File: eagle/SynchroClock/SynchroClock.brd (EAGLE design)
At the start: 84.8 x 45.7 mm, 38 parts, among them IC1 MCP1702-18, IC2 DS3231/SO, J1 VIN, U1 TC1262, U2 DRV8838, U3 ATTINY85-P

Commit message: switch to 1.5v for clock voltage regulator
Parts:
- IC1: value MCP1702-18 -> MCP1702-15
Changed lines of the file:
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@@
 <?xml version="1.0" encoding="utf-8"?>
 <!DOCTYPE eagle SYSTEM "eagle.dtd">
-<eagle version="8.2.1">
+<eagle version="8.2.2">
 <drawing>
 <settings>
@@
 <element name="C9" library="capacitor-wima" library_urn="urn:adsk.eagle:library:116" package="C2.5-2" value="0.1uf" x="31.75" y="17.78" rot="R90"/>
 <element name="IC2" library="SynchroClock" package="SO16W" value="DS3231/SO" x="77.47" y="15.24"/>
-<element name="IC1" library="SynchroClock" package="TO92-INLINE" value="MCP1702-18" x="12.7" y="8.89"/>
+<element name="IC1" library="SynchroClock" package="TO92-INLINE" value="MCP1702-15" x="12.7" y="8.89"/>
 <element name="JP2" library="pinhead" library_urn="urn:adsk.eagle:library:325" package="1X02" value="CLOCK" x="29.21" y="3.81" rot="R180"/>
 <element name="LED1" library="led" library_urn="urn:adsk.eagle:library:259" package="LED3MM" value="RED" x="3.81" y="34.29"/>

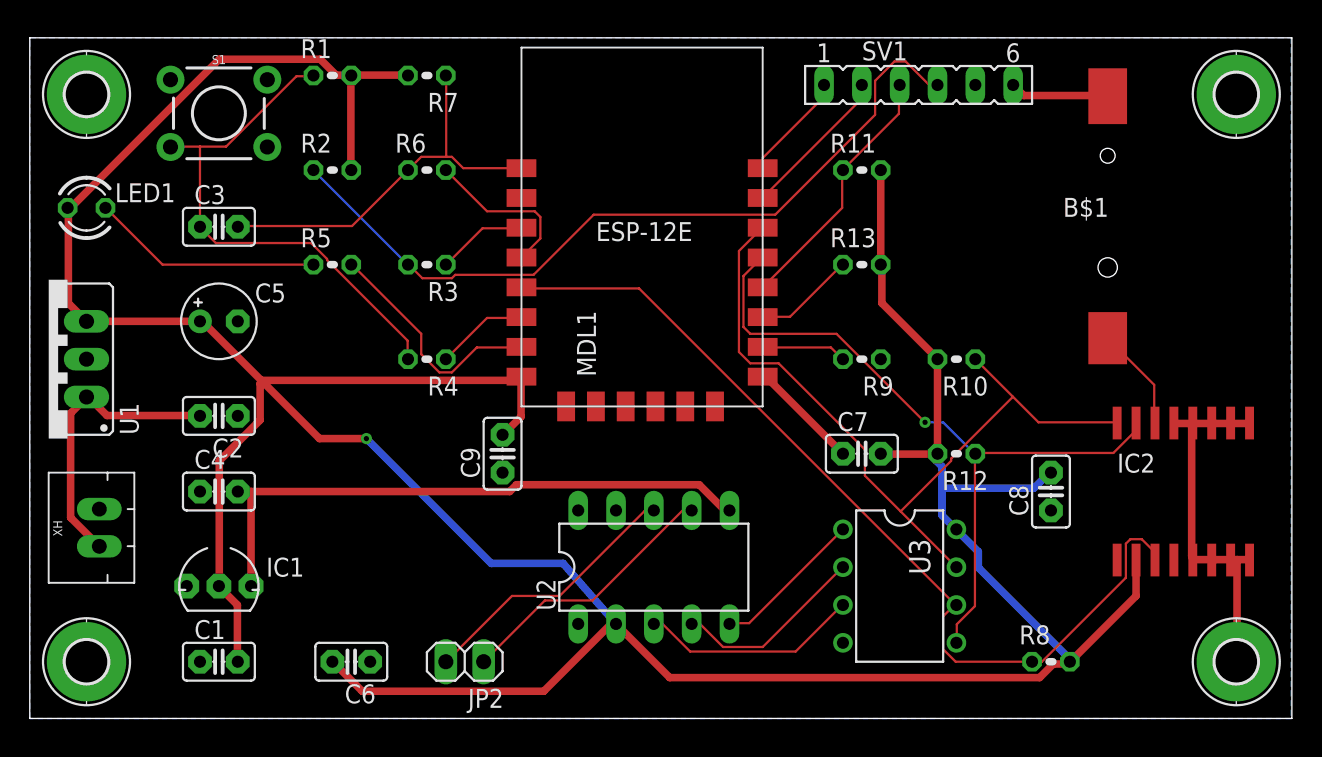
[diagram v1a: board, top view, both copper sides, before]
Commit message: "development" version - board that does not have the clock driver
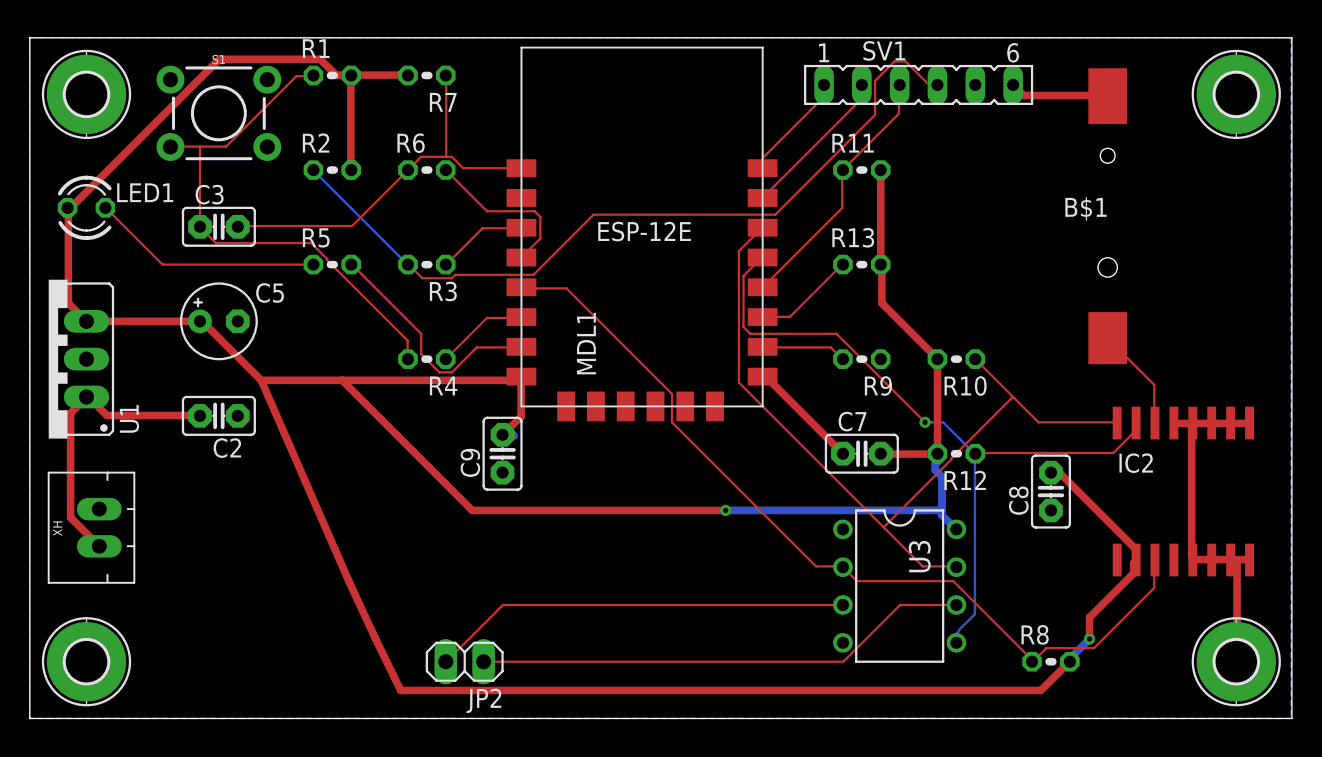
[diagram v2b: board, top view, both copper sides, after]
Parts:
- removed C1, C4, C6: 0.1uf, capacitor-wima:C2.5-2
- removed IC1: MCP1702-15, SynchroClock:TO92-INLINE
- removed U2: DRV8838, SynchroClock:DIL10
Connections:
- removed net +1V8: C4.2, IC1.3, U2.6
- removed net EN: U2.3, U3.3
- removed net N$12: JP2.1, U2.7
- removed net N$13: JP2.2, U2.8
- removed net PH: U2.4, U3.2
- removed net SLP: U2.5, U3.1
- removed net VIN: U2.9
- new net A: JP2.1, U3.6
- new net B: JP2.2, U3.3
- net +3V3: no longer C1.2, C6.2, IC1.2, U2.2
- net 1HZ: now also U3.2; no longer U3.6
- net GND: no longer C1.1, C4.1, C6.1, IC1.1, U2.1, U2.10
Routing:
- net +1V8: track 40.3 -> 0.00 mm
- net A: track 0.00 -> 33.3 mm
- net B: track 0.00 -> 28.2 mm
- net N$13: track 18.2 -> 0.00 mm
- net N$12: track 18.2 -> 0.00 mm
- net EN: track 14.8 -> 0.00 mm
- net PH: track 13.0 -> 0.00 mm
- net SLP: track 10.3 -> 0.00 mm
- net 1HZ: track 61.7 -> 58.1 mm
- net +3V3: track 242.0 -> 238.6 mm, vias 1 -> 2
- net SCL: track 52.8 -> 54.5 mm
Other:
- board text added: "SynchroClock 2.0-Dev"
- board text removed: "SynchroClock 1.0"

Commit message: Alpha 2.0 board
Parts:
- removed B$1: CR1220, SynchroClock:HARWIN-CR1220
- removed C7, C8, C9: 0.1uf, capacitor-wima:C2.5-2
- removed IC2: DS3231/SO, SynchroClock:SO16W
- removed U3: ATTINY85-P, SynchroClock:PDIP08_300MIL
- added B1: CR1220, SynchroClock:HARWIN-CR1220
- added C1: 10uf, capacitor-wima:C5B2.5
- added C4, C6: 0.1uf, capacitor-wima:C2.5-2
- added IC1: DS3231/SO, SynchroClock:SO16W
- added ISP1: AVRISP-6, SynchroClock:AVRISP
- added JP1: PWF, SynchroClock:1X02
- added JP3: ATVCC, SynchroClock:1X02
- added R14, R15: 100, resistor:0204V
- added U2: ATTINY85-P, SynchroClock:PDIP08_300MIL
- C3: value 10uf -> 100uf; device capacitor-wima:C2.5-2 -> rcl:E2,5-5
- C5: value 100uf -> 0.1uf; device rcl:E2,5-5 -> capacitor-wima:C2.5-2
- R11: value 10k -> 4.7k
- R12: value 4.7k -> 10k
- R2, R7: value 10k -> 1k
- R3, R6: value 1k -> 10k
- S1: value MOMENTARY-SWITCH-SPST-PTH-6.0MM -> CONFIG
- moved C5 56.7 mm to (68.8, 18.8), turned to 180 degrees
- moved R11 26.3 mm to (39.9, 16.0), turned to 180 degrees
- moved SV1 25.1 mm to (81.5, 30.1), turned to 90 degrees
- moved R12 20.1 mm to (55.9, 36.8), turned to 0 degrees
- moved JP2 14.7 mm to (14.5, 3.56)
- moved R8 14.7 mm to (56.1, 11.7)
- moved R2 14.2 mm to (26.7, 24.1), turned to 180 degrees
- moved R3 12.7 mm to (26.7, 43.2)
- moved R4 12.7 mm to (26.7, 36.8), turned to 0 degrees
- moved R7 12.7 mm to (26.7, 30.5)
- moved R10 9.34 mm to (55.6, 17.5)
- moved C3 6.35 mm to (12.7, 26.7)
- moved R6 6.35 mm to (20.3, 36.8)
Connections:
- net N$10 renamed GPIO2
- net N$8 renamed GPIO15
- removed net N$2: MDL1.4, R6.2
- removed net N$3: MDL1.3, R3.1
- removed net N$4: MDL1.6, R4.1
- removed net N$5: C3.1, R1.1, R4.2, S1.3
- removed net N$7: LED1.K, R5.1
- new net ATVCC: C6.2, JP3.2, U2.8
- new net CFG: MDL1.6, R2.1
- new net CH_PD: MDL1.3, R7.1
- new net GPIO16: MDL1.4, R4.1
- new net LED: LED1.K, MDL1.7
- new net N$11: JP2.2, R15.2
- new net N$9: JP2.1, R14.2
- new net NRES: ISP1.5, JP1.1, U2.1
- new net NRST: IC1.4, JP1.2
- new net REST: C1.2, MDL1.1, R3.1, R4.2
- net +3V3: now also C3.+, C4.2, C5.2, IC1.2, ISP1.2, JP3.1, R3.2, R5.2, R6.2; no longer C5.+, C7.2, C8.2, C9.2, IC2.2, LED1.A, R2.2, R7.2, U3.8
- net 1HZ: now also IC1.3, U2.2; no longer IC2.3, U3.2
- net A: now also ISP1.1, R14.1, U2.6; no longer JP2.1, U3.6
- net B: now also R15.1, U2.3; no longer JP2.2, U3.3
- net GND: now also B1.NEG, C3.-, C4.1, C5.1, C6.1, IC1.10, IC1.11, IC1.12, IC1.13, IC1.5, IC1.6, IC1.7, IC1.8, IC1.9, ISP1.6, U2.4; no longer B$1.NEG, C5.-, C7.1, C8.1, C9.1, IC2.10, IC2.11, IC2.12, IC2.13, IC2.5, IC2.6, IC2.7, IC2.8, IC2.9, U3.4
- net GPIO0: now also R12.1; no longer R11.1
- net N$1: now also C1.1, R1.1, R2.2, S1.3; no longer C3.2, MDL1.1, R6.1, R7.1
- net N$6: now also LED1.A, R5.1; no longer MDL1.7, R5.2
- net RST: now also R6.1, R7.2; no longer R2.1, R3.2
- net SCL: now also IC1.16, ISP1.3, U2.7; no longer IC2.16, U3.7
- net SDA: now also IC1.15, ISP1.4, R11.1, U2.5; no longer IC2.15, R12.1, U3.5
- net VBAT: now also B1.POS, IC1.14; no longer B$1.POS, IC2.14
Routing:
- net +3V3: track 238.6 -> 149.3 mm, vias 2 -> 0
- net SDA: track 49.5 -> 95.6 mm
- net GPIO0: track 17.4 -> 57.0 mm
- net TXD: track 7.30 -> 44.1 mm
- net NRES: track 0.00 -> 36.5 mm
- net LED: track 0.00 -> 36.2 mm
- net N$5: track 35.4 -> 0.00 mm
- net SCL: track 54.5 -> 87.9 mm, vias 0 -> 1
- net REST: track 0.00 -> 25.9 mm
- net RXD: track 10.3 -> 35.9 mm
- net RST: track 53.0 -> 71.8 mm
- net B: track 28.2 -> 12.3 mm
- net N$7: track 15.5 -> 0.00 mm
- net ATVCC: track 0.00 -> 15.5 mm
- net 1HZ: track 58.1 -> 72.6 mm
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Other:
- board text added: "SynchroClock 2.0-Alpha"
- board text removed: "SynchroClock 2.0-Dev"

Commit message: added power fail circuit for ATtiny85 added BOM save all clock properties at power fail
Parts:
- removed JP3: ATVCC, SynchroClock:1X02
- added C7: 220uf, rcl:E2,5-5
- added D1: BAT46, SynchroClock:DO35-10
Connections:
- net +3V3: now also D1.A; no longer JP3.1
- net ATVCC: now also C7.+, D1.C; no longer JP3.2
- net GND: now also C7.-
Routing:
- net ATVCC: track 15.5 -> 26.5 mm
- net +3V3: track 149.3 -> 154.5 mm
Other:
- board text added: "SynchroClock 2.0"
- board text removed: "SynchroClock 2.0-Alpha"
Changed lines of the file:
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@@
 <wire x1="84.76" y1="45.71" x2="0" y2="45.71" width="0" layer="20"/>
 <wire x1="0" y1="45.71" x2="0" y2="0" width="0" layer="20"/>
-<text x="77.216" y="41.148" size="1.778" layer="22" rot="MR0">SynchroClock 2.0-Alpha</text>
+<text x="77.216" y="41.148" size="1.778" layer="22" rot="MR0">SynchroClock 2.0</text>
 </plain>
 <attributes>
@@
 <element name="R14" library="resistor" library_urn="urn:adsk.eagle:library:348" package="0204V" value="100" x="17.272" y="9.652" rot="R180"/>
 <element name="R15" library="resistor" library_urn="urn:adsk.eagle:library:348" package="0204V" value="100" x="11.43" y="9.652" rot="R180"/>
-<element name="JP3" library="SynchroClock" package="1X02" value="ATVCC" x="19.812" y="17.78"/>
 <element name="JP1" library="SynchroClock" package="1X02" value="PWF" x="55.118" y="4.064"/>
 <element name="ISP1" library="SynchroClock" package="AVRISP" value="AVRISP-6" x="44.196" y="4.318" rot="R270"/>
+<element name="D1" library="SynchroClock" package="DO35-10" value="BAT46" x="20.828" y="17.272" rot="R180"/>
+<element name="C7" library="rcl" library_urn="urn:adsk.eagle:library:334" package="E2,5-5" value="220uf" x="12.7" y="14.732" rot="R180"/>
 </elements>
 <signals>
@@
 <contactref element="R11" pad="2"/>
 <contactref element="R8" pad="2"/>
-<contactref element="JP3" pad="1"/>
 <contactref element="ISP1" pad="2"/>
 <contactref element="R1" pad="2"/>
@@
 <wire x1="11.43" y1="26.67" x2="12.6492" y2="27.8892" width="0.508" layer="1"/>
 <wire x1="11.43" y1="26.67" x2="3.81" y2="26.67" width="0.508" layer="1"/>
-<wire x1="19.812" y1="25.908" x2="19.812" y2="20.193" width="0.508" layer="1"/>
-<wire x1="19.812" y1="20.193" x2="19.812" y2="17.78" width="0.508" layer="1"/>
-<wire x1="18.0594" y1="27.6606" x2="19.812" y2="25.908" width="0.508" layer="1"/>
+<wire x1="22.098" y1="24.13" x2="26.416" y2="20.193" width="0.508" layer="1"/>
+<wire x1="18.0594" y1="27.6606" x2="22.098" y2="24.13" width="0.508" layer="1"/>
 <wire x1="18.0594" y1="27.6606" x2="17.9832" y2="27.8892" width="0.508" layer="1"/>
 <wire x1="21.5646" y1="36.2712" x2="21.5646" y2="36.6522" width="0.508" layer="16"/>
@@
 <wire x1="21.5646" y1="36.6522" x2="21.59" y2="36.83" width="0.508" layer="16"/>
 <wire x1="21.6408" y1="30.48" x2="21.59" y2="30.48" width="0.508" layer="16"/>
-<wire x1="19.812" y1="20.193" x2="29.9466" y2="20.193" width="0.508" layer="1"/>
+<wire x1="26.416" y1="20.193" x2="29.9466" y2="20.193" width="0.508" layer="1"/>
 <wire x1="29.9466" y1="20.193" x2="30.226" y2="20.066" width="0.508" layer="1"/>
 <wire x1="40.4622" y1="14.6304" x2="55.245" y2="14.6304" width="0.508" layer="16"/>
@@
 <wire x1="38.6334" y1="16.002" x2="38.7096" y2="15.9258" width="0.508" layer="16"/>
 <wire x1="38.6334" y1="16.002" x2="38.608" y2="16.002" width="0.508" layer="16"/>
+<contactref element="D1" pad="A"/>
+<wire x1="15.748" y1="17.272" x2="15.748" y2="22.352" width="0.508" layer="1"/>
+<wire x1="15.748" y1="22.352" x2="11.43" y2="26.67" width="0.508" layer="1"/>
 </signal>
 <signal name="GPIO16">
@@
 <wire x1="72.39" y1="5.6388" x2="72.164" y2="5.715" width="0.508" layer="1"/>
 <wire x1="81.0006" y1="3.81" x2="81.026" y2="3.81" width="0.508" layer="1"/>
+<contactref element="C7" pad="-"/>
 </signal>
 <signal name="1HZ">
@@
 <contactref element="C6" pad="2"/>
 <contactref element="U2" pad="8"/>
-<contactref element="JP3" pad="2"/>
-<wire x1="35.052" y1="11.9634" x2="30.7848" y2="11.9634" width="0.508" layer="1"/>
+<wire x1="30.7848" y1="11.9634" x2="35.052" y2="11.9634" width="0.508" layer="1"/>
 <wire x1="35.2806" y1="12.192" x2="35.052" y2="11.9634" width="0.508" layer="1"/>
 <wire x1="30.7848" y1="11.9634" x2="30.734" y2="11.938" width="0.508" layer="1"/>
 <wire x1="35.2806" y1="12.192" x2="35.306" y2="12.192" width="0.508" layer="1"/>
-<wire x1="24.9174" y1="17.7546" x2="22.4028" y2="17.7546" width="0.508" layer="1"/>
-<wire x1="30.734" y1="11.938" x2="24.9174" y2="17.7546" width="0.508" layer="1"/>
-<wire x1="22.4028" y1="17.7546" x2="22.352" y2="17.78" width="0.508" layer="1"/>
+<contactref element="D1" pad="C"/>
+<contactref element="C7" pad="+"/>
+<wire x1="25.908" y1="17.272" x2="25.908" y2="16.8402" width="0.508" layer="1"/>
+<wire x1="28.3591" y1="14.3891" x2="25.908" y2="16.8402" width="0.508" layer="1"/>
+<wire x1="28.3591" y1="14.3891" x2="30.7848" y2="11.9634" width="0.508" layer="1"/>
+<wire x1="13.97" y1="14.732" x2="28.0162" y2="14.732" width="0.508" layer="1"/>
+<wire x1="28.0162" y1="14.732" x2="28.3591" y2="14.3891" width="0.508" layer="1"/>
 </signal>
 <signal name="NRES">

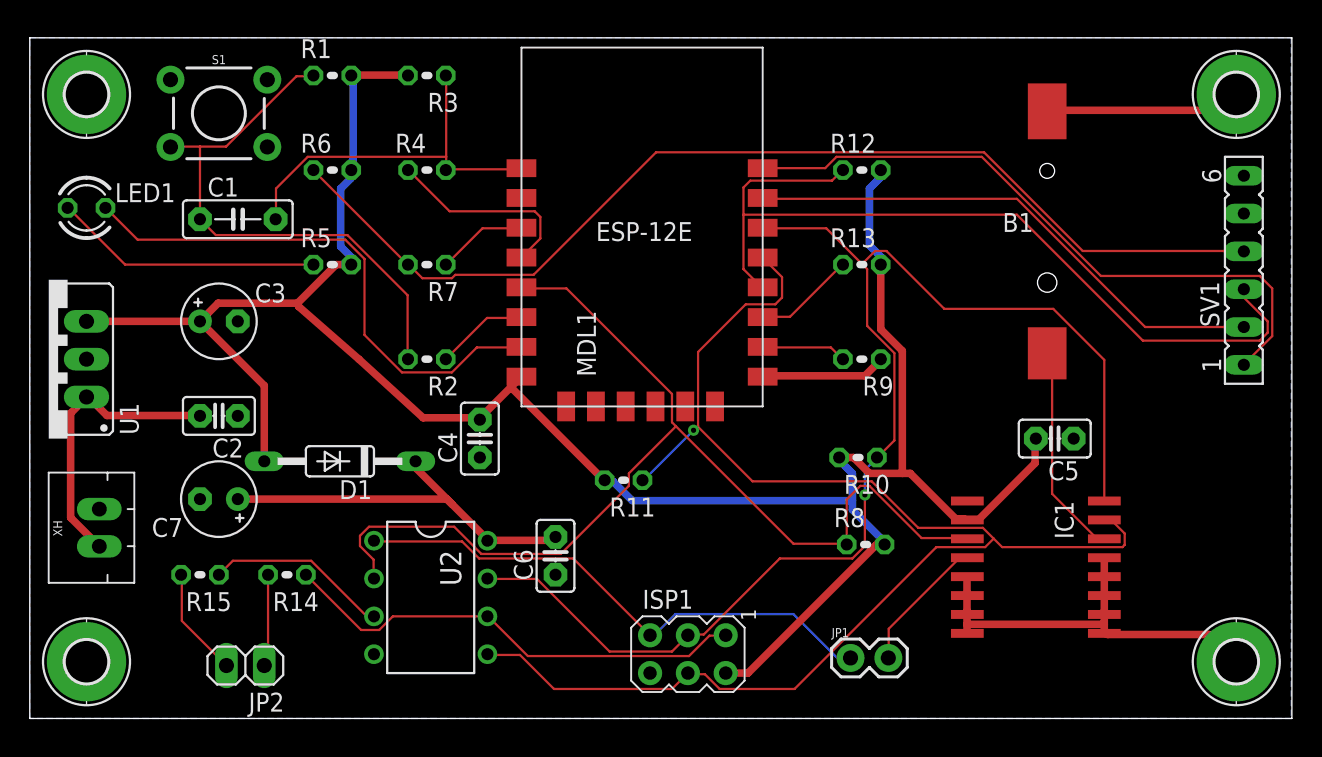
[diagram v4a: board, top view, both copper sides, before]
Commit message: updated with new voltage regulator and pwrgd signal for power fail
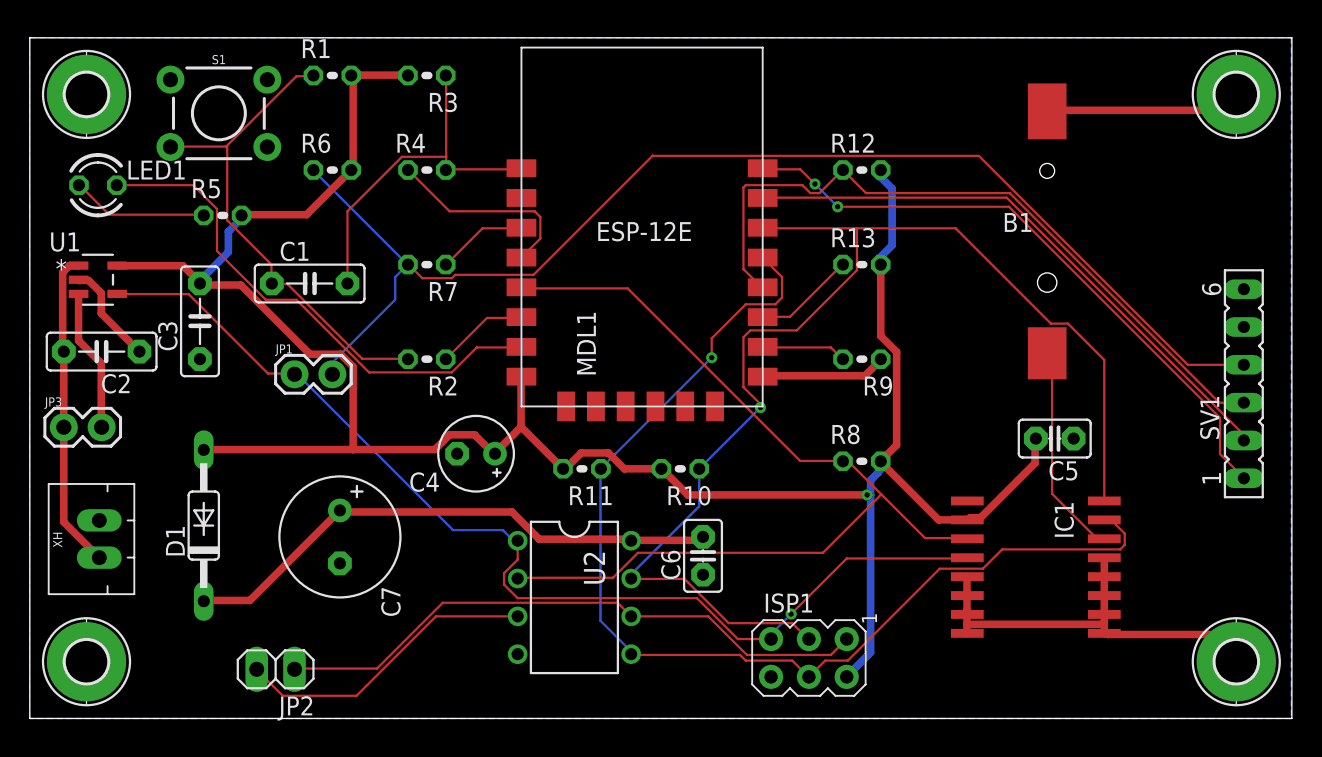
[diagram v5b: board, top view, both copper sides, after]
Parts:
- removed R14, R15: 100, resistor:0204V
- added JP3: !SHDN, SynchroClock:1X02
- C2: value 0.1uf -> 10uf; device capacitor-wima:C2.5-2 -> capacitor-wima:C5B2.5
- C3: value 100uf -> 10uf; device rcl:E2,5-5 -> capacitor-wima:C5B2.5
- C4: value 0.1uf -> 100uf; device capacitor-wima:C2.5-2 -> rcl:E2,5-5
- C7: value 220uf -> 510uf; device rcl:E2,5-5 -> rcl:E3,5-8
- JP1: value PWF -> PWRGD
- U1: value TC1262 -> MCP1755T-3302E/OT; device SynchroClock:TO220-3V -> SynchroClock:SOT-23-5_MC
- moved JP1 41.9 mm to (17.8, 23.1)
- moved R10 12.0 mm to (43.7, 16.8)
- moved D1 10.1 mm to (11.7, 13.0), turned to 90 degrees
- moved C6 9.91 mm to (45.2, 10.9)
- moved U2 9.65 mm to (36.6, 8.13)
- moved C2 8.98 mm to (4.83, 24.6)
- moved C7 8.52 mm to (20.8, 12.2), turned to 270 degrees
- moved ISP1 8.13 mm to (52.3, 4.06)
- moved R5 8.07 mm to (13.0, 33.8)
- moved SV1 7.62 mm to (81.5, 22.5)
- moved C1 6.48 mm to (18.8, 29.2)
- moved U1 6.27 mm to (4.57, 29.5), turned to 0 degrees
- moved R8 5.59 mm to (55.9, 17.3)
- moved R11 2.90 mm to (37.1, 16.8)
- moved JP2 2.05 mm to (16.5, 3.30)
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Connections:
- removed net N$11: JP2.2, R15.2
- removed net N$9: JP2.1, R14.2
- removed net NRES: ISP1.5, JP1.1, U2.1
- removed net NRST: IC1.4, JP1.2
- new net !SHDN: JP3.2, U1.3
- new net PWRGD: IC1.4, ISP1.5, JP1.1, U1.4, U2.1
- net +3V3: now also C3.2, C4.+, U1.5; no longer C3.+, C4.2, U1.3
- net +5V: now also JP3.1
- net A: now also JP2.1; no longer R14.1
- net B: now also JP2.2; no longer R15.1
- net GND: now also C3.1, C4.-; no longer C3.-, C4.1
- net RST: now also JP1.2
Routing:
- net PWRGD: track 0.00 -> 72.2 mm, vias 0 -> 1
- net NRES: track 36.5 -> 0.00 mm
- net SDA: track 95.6 -> 74.2 mm
- net RST: track 71.8 -> 84.2 mm
- net ATVCC: track 26.5 -> 37.0 mm
- net !SHDN: track 0.00 -> 9.60 mm
- net NRST: track 9.23 -> 0.00 mm
- net A: track 31.8 -> 40.8 mm
- net 1HZ: track 72.6 -> 63.8 mm
- net N$6: track 18.1 -> 9.23 mm
- net GPIO0: track 57.0 -> 48.3 mm
- net B: track 12.3 -> 20.5 mm
- net N$11: track 7.36 -> 0.00 mm
- net GND: track 49.5 -> 56.4 mm
- net N$9: track 6.20 -> 0.00 mm
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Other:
- board text added: "SynchroClock 2.1"
- board text removed: "SynchroClock 2.0"
